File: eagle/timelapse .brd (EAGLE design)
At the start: 47.9 x 33 mm, 11 parts, among them U1 ATTINY2313V-10PU, X1 1501_04

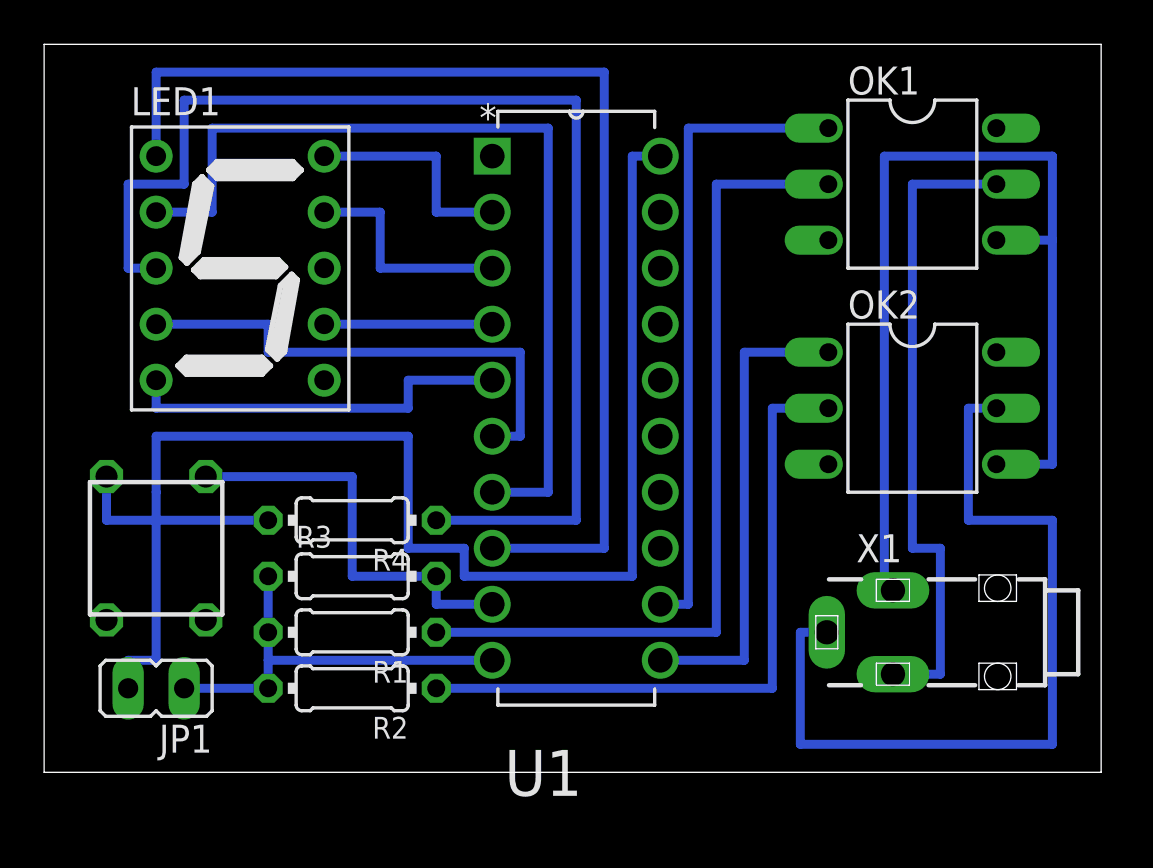
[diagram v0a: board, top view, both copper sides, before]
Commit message: change of board layout - smaller
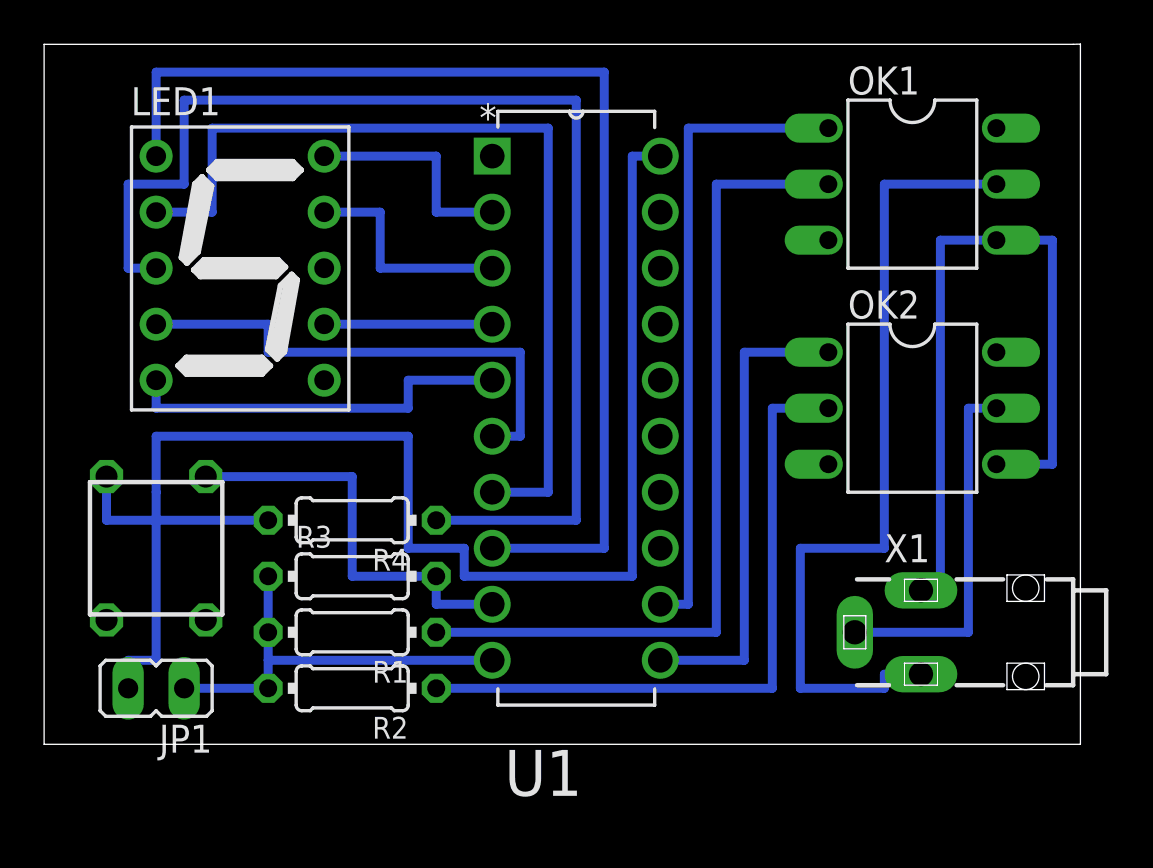
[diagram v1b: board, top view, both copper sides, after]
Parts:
- moved X1 1.27 mm to (45.7, 22.9)
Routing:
- net N$19: track 38.0 -> 16.6 mm
- net N$16: track 46.8 -> 34.5 mm
- net N$18: track 29.5 -> 37.9 mm
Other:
- board size 47.9 x 33 mm -> 47 x 31.8 mm
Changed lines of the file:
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@@
 <board>
 <plain>
-<wire x1="-2.54" y1="16.51" x2="45.39" y2="16.51" width="0" layer="20"/>
-<wire x1="45.39" y1="16.51" x2="45.39" y2="49.52" width="0" layer="20"/>
-<wire x1="45.39" y1="49.52" x2="-2.54" y2="49.52" width="0" layer="20"/>
-<wire x1="-2.54" y1="49.52" x2="-2.54" y2="16.51" width="0" layer="20"/>
+<wire x1="-2.54" y1="17.78" x2="44.45" y2="17.78" width="0" layer="20"/>
+<wire x1="44.45" y1="17.78" x2="44.45" y2="49.53" width="0" layer="20"/>
+<wire x1="44.45" y1="49.53" x2="44.12" y2="49.52" width="0" layer="20"/>
+<wire x1="44.12" y1="49.52" x2="-2.54" y2="49.52" width="0" layer="20"/>
+<wire x1="-2.54" y1="49.52" x2="-2.54" y2="17.78" width="0" layer="20"/>
 </plain>
 <attributes>
@@
 <attribute name="SPICEPREFIX" value="R" x="11.43" y="22.86" size="1.778" layer="27" rot="R180" display="off"/>
 </element>
-<element name="X1" library="con-lumberg" package="1501_05" value="1501_04" x="44.45" y="22.86" rot="R270">
-<attribute name="OC_NEWARK" value="unknown" x="44.45" y="22.86" size="1.778" layer="27" rot="R270" display="off"/>
-<attribute name="MPN" value="" x="44.45" y="22.86" size="1.778" layer="27" rot="R270" display="off"/>
-<attribute name="MF" value="" x="44.45" y="22.86" size="1.778" layer="27" rot="R270" display="off"/>
-<attribute name="OC_FARNELL" value="1216977" x="44.45" y="22.86" size="1.778" layer="27" rot="R270" display="off"/>
+<element name="X1" library="con-lumberg" package="1501_05" value="1501_04" x="45.72" y="22.86" rot="R270">
+<attribute name="OC_NEWARK" value="unknown" x="45.72" y="22.86" size="1.778" layer="27" rot="R270" display="off"/>
+<attribute name="MPN" value="" x="45.72" y="22.86" size="1.778" layer="27" rot="R270" display="off"/>
+<attribute name="MF" value="" x="45.72" y="22.86" size="1.778" layer="27" rot="R270" display="off"/>
+<attribute name="OC_FARNELL" value="1216977" x="45.72" y="22.86" size="1.778" layer="27" rot="R270" display="off"/>
 </element>
 <element name="JP1" library="jumper" package="JP1" value="Battery" x="2.54" y="20.32" rot="R90"/>
@@
 <contactref element="X1" pad="1"/>
 <contactref element="OK2" pad="4"/>
-<wire x1="35.95" y1="24.76" x2="35.56" y2="24.76" width="0.4064" layer="16"/>
-<wire x1="35.56" y1="24.76" x2="35.56" y2="44.45" width="0.4064" layer="16"/>
-<wire x1="35.56" y1="44.45" x2="43.18" y2="44.45" width="0.4064" layer="16"/>
-<wire x1="43.18" y1="44.45" x2="43.18" y2="40.64" width="0.4064" layer="16"/>
+<wire x1="37.22" y1="24.76" x2="38.1" y2="24.76" width="0.4064" layer="16"/>
+<wire x1="38.1" y1="24.76" x2="38.1" y2="40.64" width="0.4064" layer="16"/>
+<wire x1="38.1" y1="40.64" x2="40.64" y2="40.64" width="0.4064" layer="16"/>
 <wire x1="43.18" y1="40.64" x2="40.64" y2="40.64" width="0.4064" layer="16"/>
 <wire x1="40.64" y1="30.48" x2="43.18" y2="30.48" width="0.4064" layer="16"/>
@@
 <contactref element="X1" pad="3"/>
 <contactref element="OK1" pad="5"/>
-<wire x1="40.64" y1="43.18" x2="36.83" y2="43.18" width="0.4064" layer="16"/>
-<wire x1="36.83" y1="43.18" x2="36.83" y2="26.67" width="0.4064" layer="16"/>
-<wire x1="36.83" y1="26.67" x2="38.1" y2="26.67" width="0.4064" layer="16"/>
-<wire x1="38.1" y1="26.67" x2="38.1" y2="20.96" width="0.4064" layer="16"/>
-<wire x1="38.1" y1="20.96" x2="35.95" y2="20.96" width="0.4064" layer="16"/>
+<wire x1="40.64" y1="43.18" x2="35.56" y2="43.18" width="0.4064" layer="16"/>
+<wire x1="35.56" y1="43.18" x2="35.56" y2="26.67" width="0.4064" layer="16"/>
+<wire x1="35.56" y1="26.67" x2="31.75" y2="26.67" width="0.4064" layer="16"/>
+<wire x1="31.75" y1="26.67" x2="31.75" y2="20.32" width="0.4064" layer="16"/>
+<wire x1="37.22" y1="20.96" x2="35.56" y2="20.96" width="0.4064" layer="16"/>
+<wire x1="35.56" y1="20.96" x2="35.56" y2="20.32" width="0.4064" layer="16"/>
+<wire x1="35.56" y1="20.32" x2="31.75" y2="20.32" width="0.4064" layer="16"/>
 </signal>
 <signal name="N$19">
 <contactref element="X1" pad="2"/>
 <contactref element="OK2" pad="5"/>
-<wire x1="32.95" y1="22.86" x2="31.75" y2="22.86" width="0.4064" layer="16"/>
-<wire x1="31.75" y1="22.86" x2="31.75" y2="17.78" width="0.4064" layer="16"/>
-<wire x1="31.75" y1="17.78" x2="43.18" y2="17.78" width="0.4064" layer="16"/>
-<wire x1="43.18" y1="17.78" x2="43.18" y2="27.94" width="0.4064" layer="16"/>
-<wire x1="43.18" y1="27.94" x2="39.37" y2="27.94" width="0.4064" layer="16"/>
-<wire x1="39.37" y1="27.94" x2="39.37" y2="33.02" width="0.4064" layer="16"/>
+<wire x1="34.22" y1="22.86" x2="39.37" y2="22.86" width="0.4064" layer="16"/>
+<wire x1="39.37" y1="22.86" x2="39.37" y2="33.02" width="0.4064" layer="16"/>
 <wire x1="39.37" y1="33.02" x2="40.64" y2="33.02" width="0.4064" layer="16"/>
 </signal>
